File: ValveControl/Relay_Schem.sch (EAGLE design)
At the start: 69 parts, among them M1 IRLZ44, M2 IRLZ44, M3 IRLZ44, M4 IRLZ44, Q1 LINEAR_REGULATOR, Q2 LINEAR_REGULATOR, Q3 LINEAR_REGULATOR, Q4 LINEAR_REGULATOR, Q5 LINEAR_REGULATOR

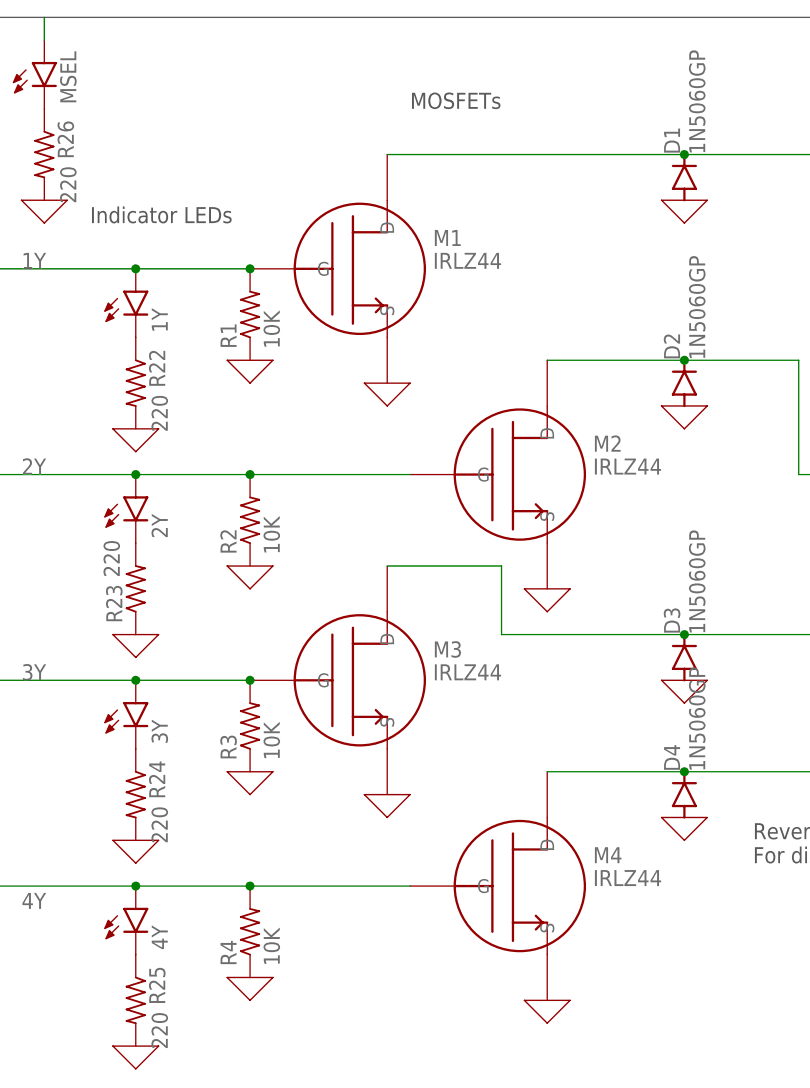
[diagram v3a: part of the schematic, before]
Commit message: Fix schematic errors, finish board layout
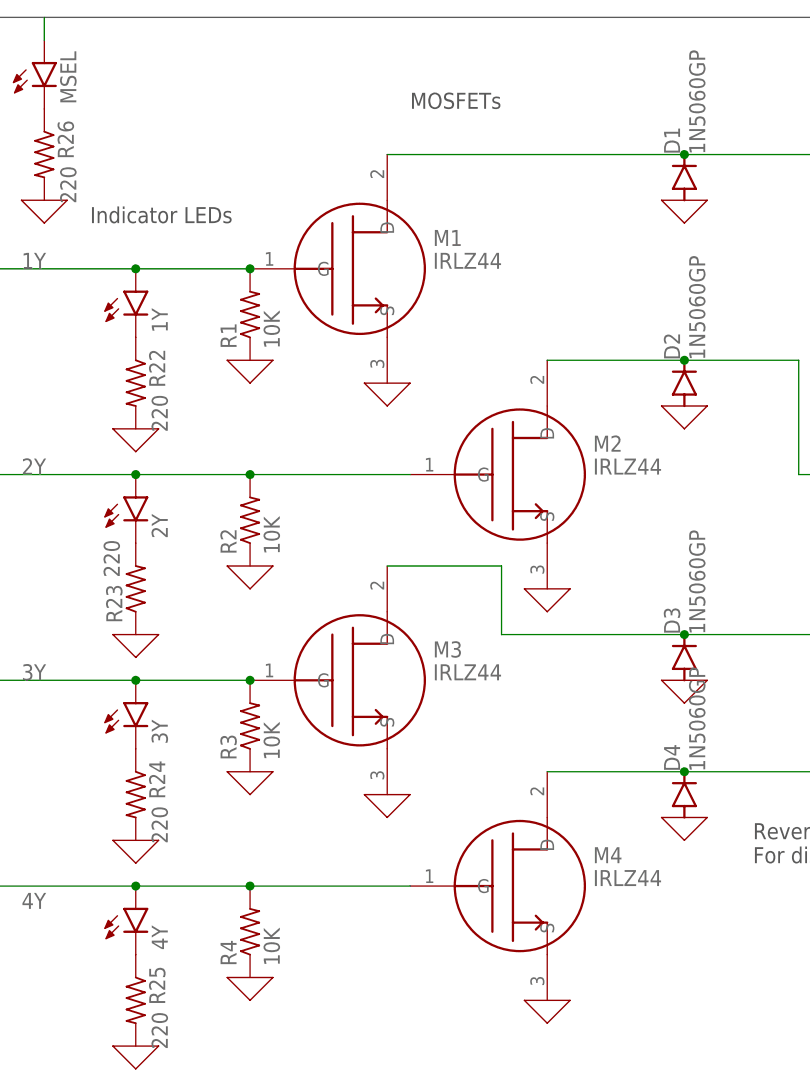
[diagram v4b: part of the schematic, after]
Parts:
- M1, M2, M3, M4: device ngspice-simulation:FET_N -> LPRD_RELAY:FET_N

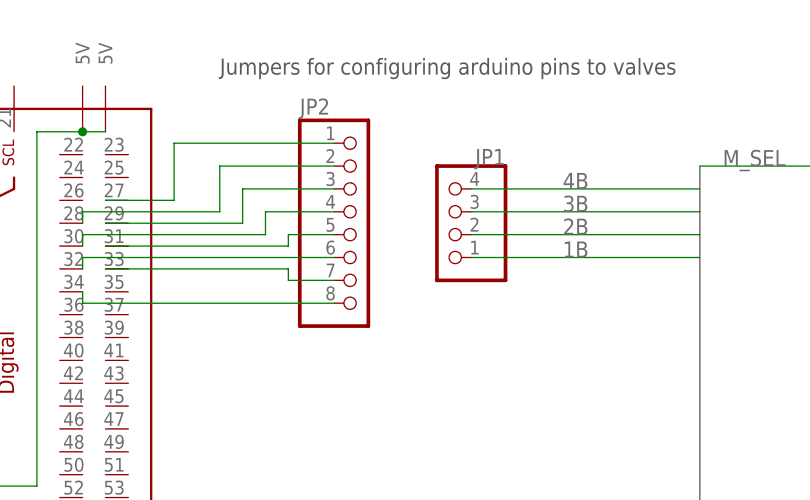
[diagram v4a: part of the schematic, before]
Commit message: Add pin numbers to valve pin selection jumper header
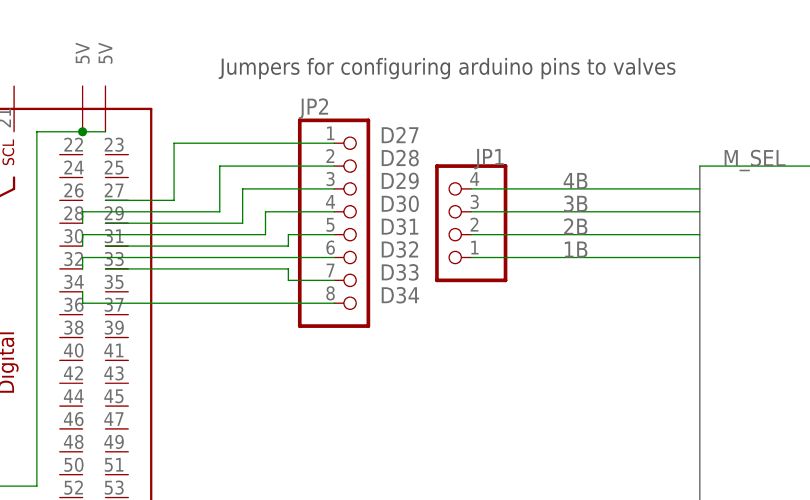
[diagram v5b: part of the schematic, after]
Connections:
- net N$25 renamed D27
- net N$26 renamed D28
- net N$27 renamed D29
- net N$28 renamed D30
- net N$29 renamed D31
- net N$30 renamed D32
- net N$31 renamed D33
- net N$32 renamed D34
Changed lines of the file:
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@@
 </segment>
 </net>
-<net name="N$25" class="0">
+<net name="D27" class="0">
 <segment>
 <pinref part="U$2" gate="G$1" pin="27"/>
@@
 <pinref part="JP2" gate="A" pin="1"/>
 <wire x1="48.26" y1="165.1" x2="66.04" y2="165.1" width="0.1524" layer="91"/>
+<label x="71.12" y="165.1" size="1.778" layer="95"/>
 </segment>
 </net>
-<net name="N$26" class="0">
+<net name="D28" class="0">
 <segment>
 <pinref part="U$2" gate="G$1" pin="28"/>
@@
 <pinref part="JP2" gate="A" pin="2"/>
 <wire x1="53.34" y1="162.56" x2="66.04" y2="162.56" width="0.1524" layer="91"/>
+<label x="71.12" y="162.56" size="1.778" layer="95"/>
 </segment>
 </net>
-<net name="N$27" class="0">
+<net name="D29" class="0">
 <segment>
 <pinref part="U$2" gate="G$1" pin="29"/>
@@
 <pinref part="JP2" gate="A" pin="3"/>
 <wire x1="55.88" y1="160.02" x2="66.04" y2="160.02" width="0.1524" layer="91"/>
+<label x="71.12" y="160.02" size="1.778" layer="95"/>
 </segment>
 </net>
-<net name="N$28" class="0">
+<net name="D30" class="0">
 <segment>
 <pinref part="U$2" gate="G$1" pin="30"/>
@@
 <pinref part="JP2" gate="A" pin="4"/>
 <wire x1="58.42" y1="157.48" x2="66.04" y2="157.48" width="0.1524" layer="91"/>
+<label x="71.12" y="157.48" size="1.778" layer="95"/>
 </segment>
 </net>
-<net name="N$29" class="0">
+<net name="D31" class="0">
 <segment>
 <pinref part="U$2" gate="G$1" pin="31"/>
@@
 <pinref part="JP2" gate="A" pin="5"/>
 <wire x1="60.96" y1="154.94" x2="66.04" y2="154.94" width="0.1524" layer="91"/>
+<label x="71.12" y="154.94" size="1.778" layer="95"/>
 </segment>
 </net>
-<net name="N$30" class="0">
+<net name="D32" class="0">
 <segment>
 <pinref part="U$2" gate="G$1" pin="32"/>
@@
 <wire x1="38.1" y1="151.13" x2="38.1" y2="152.4" width="0.1524" layer="91"/>
 <wire x1="38.1" y1="152.4" x2="66.04" y2="152.4" width="0.1524" layer="91"/>
+<label x="71.12" y="152.4" size="1.778" layer="95"/>
 </segment>
 </net>
-<net name="N$31" class="0">
+<net name="D33" class="0">
 <segment>
 <pinref part="U$2" gate="G$1" pin="33"/>
@@
 <pinref part="JP2" gate="A" pin="7"/>
 <wire x1="60.96" y1="149.86" x2="66.04" y2="149.86" width="0.1524" layer="91"/>
+<label x="71.12" y="149.86" size="1.778" layer="95"/>
 </segment>
 </net>
-<net name="N$32" class="0">
+<net name="D34" class="0">
 <segment>
 <pinref part="U$2" gate="G$1" pin="34"/>
@@
 <wire x1="38.1" y1="148.59" x2="38.1" y2="147.32" width="0.1524" layer="91"/>
 <wire x1="38.1" y1="147.32" x2="66.04" y2="147.32" width="0.1524" layer="91"/>
+<label x="71.12" y="147.32" size="1.778" layer="95"/>
 </segment>
 </net>

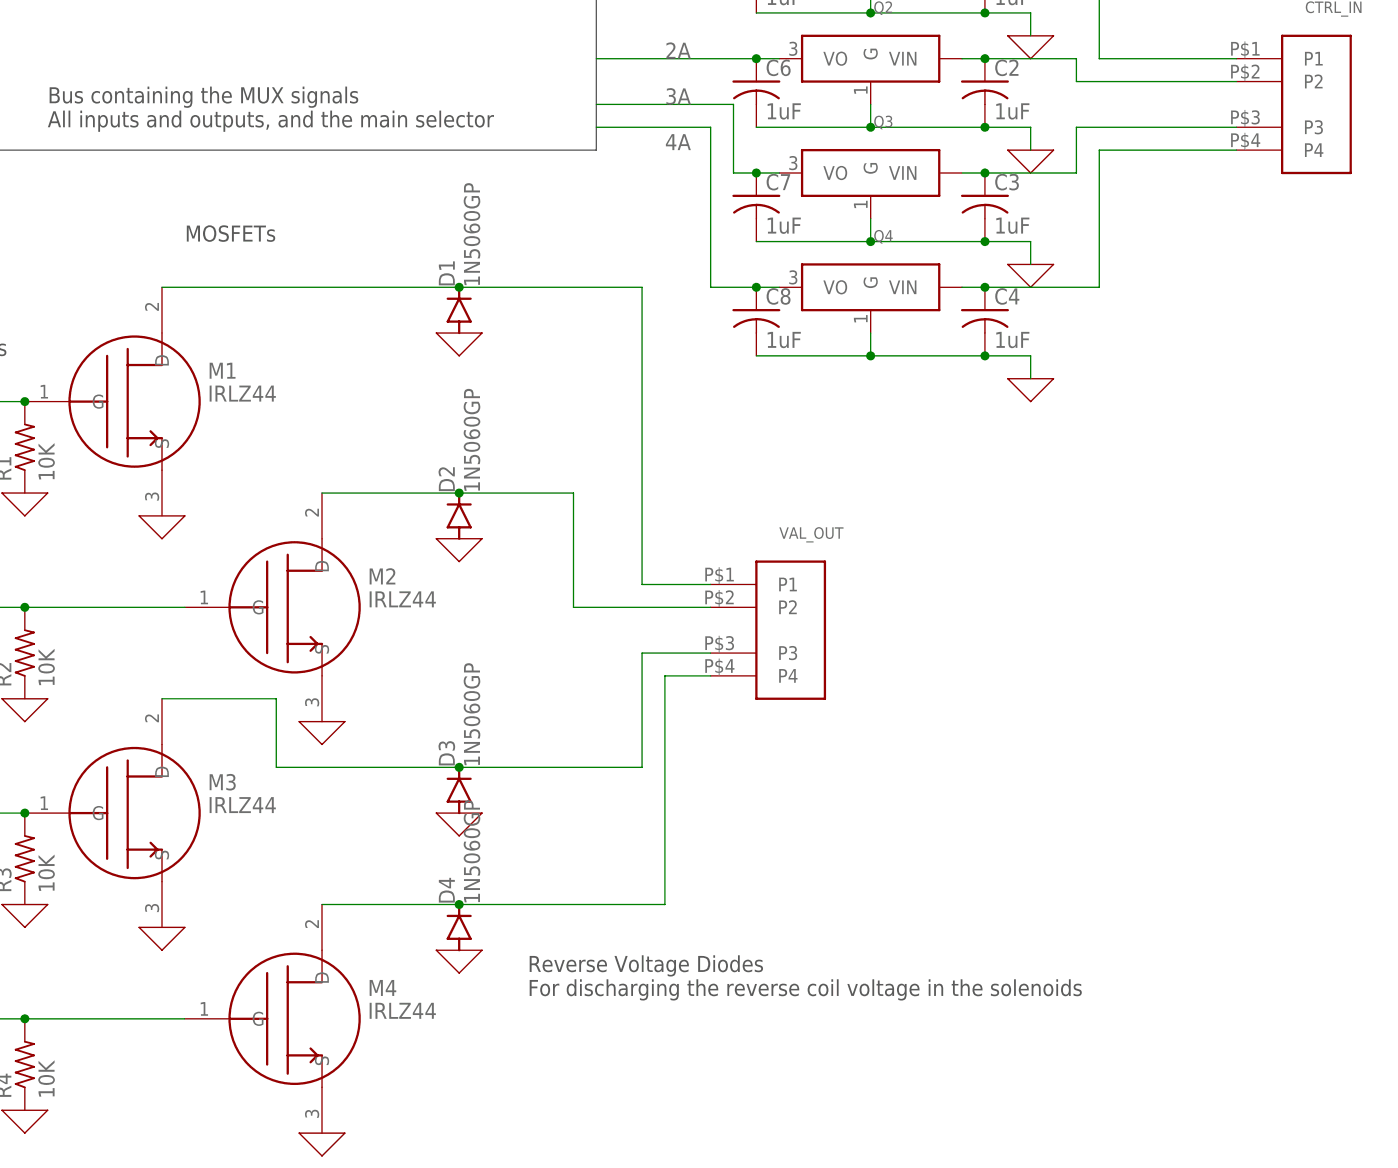
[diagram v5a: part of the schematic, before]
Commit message: Remove diodes, fix some slight layout issues
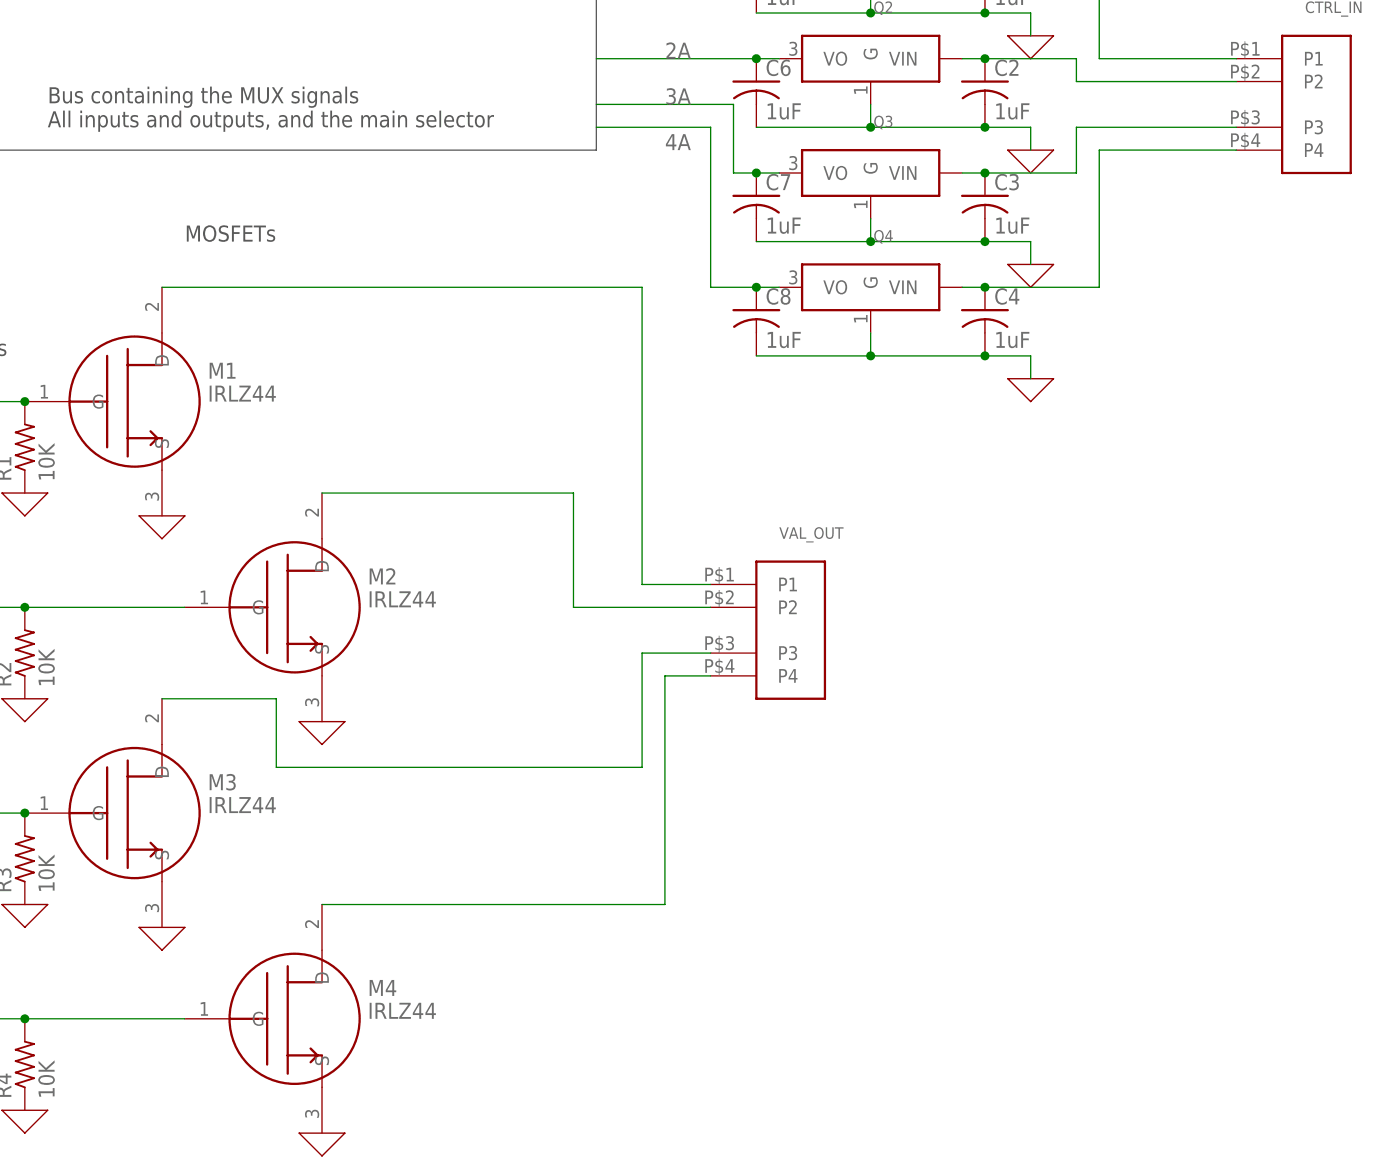
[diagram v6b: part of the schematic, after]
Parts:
- removed D1, D2, D3, D4: 1N5060GP, diode:1N5060GP
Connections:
- net 0: no longer D1.A, D2.A, D3.A, D4.A
- net N$3: no longer D1.C
- net N$5: no longer D2.C
- net N$8: no longer D3.C
- net N$9: no longer D4.C
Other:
- note removed: "Reverse Voltage Diodes For discharging the reverse coil voltage in the solenoids"
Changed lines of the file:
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@@
 <part name="R24" library="rcl" library_urn="urn:adsk.eagle:library:334" deviceset="R-US_" device="0204/7" package3d_urn="urn:adsk.eagle:package:23498/2" value="220"/>
 <part name="R25" library="rcl" library_urn="urn:adsk.eagle:library:334" deviceset="R-US_" device="0204/7" package3d_urn="urn:adsk.eagle:package:23498/2" value="220"/>
-<part name="D1" library="diode" library_urn="urn:adsk.eagle:library:210" deviceset="1N5060GP" device="" package3d_urn="urn:adsk.eagle:package:43369/2"/>
-<part name="D2" library="diode" library_urn="urn:adsk.eagle:library:210" deviceset="1N5060GP" device="" package3d_urn="urn:adsk.eagle:package:43369/2"/>
-<part name="D3" library="diode" library_urn="urn:adsk.eagle:library:210" deviceset="1N5060GP" device="" package3d_urn="urn:adsk.eagle:package:43369/2"/>
-<part name="D4" library="diode" library_urn="urn:adsk.eagle:library:210" deviceset="1N5060GP" device="" package3d_urn="urn:adsk.eagle:package:43369/2"/>
-<part name="X_15" library="ngspice-simulation" library_urn="urn:adsk.eagle:library:527439" deviceset="GND" device=""/>
 <part name="MSEL" library="led" library_urn="urn:adsk.eagle:library:259" deviceset="LED" device="3MM" package3d_urn="urn:adsk.eagle:package:15797/1"/>
 <part name="R26" library="rcl" library_urn="urn:adsk.eagle:library:334" deviceset="R-US_" device="0204/7" package3d_urn="urn:adsk.eagle:package:23498/2" value="220"/>
@@
 <part name="X_25" library="ngspice-simulation" library_urn="urn:adsk.eagle:library:527439" deviceset="GND" device=""/>
 <part name="X_26" library="ngspice-simulation" library_urn="urn:adsk.eagle:library:527439" deviceset="GND" device=""/>
-<part name="X_27" library="ngspice-simulation" library_urn="urn:adsk.eagle:library:527439" deviceset="GND" device=""/>
-<part name="X_28" library="ngspice-simulation" library_urn="urn:adsk.eagle:library:527439" deviceset="GND" device=""/>
-<part name="X_29" library="ngspice-simulation" library_urn="urn:adsk.eagle:library:527439" deviceset="GND" device=""/>
 <part name="JP1" library="pinhead" library_urn="urn:adsk.eagle:library:325" deviceset="PINHD-1X4" device="" package3d_urn="urn:adsk.eagle:package:22407/2"/>
 <part name="JP2" library="pinhead" library_urn="urn:adsk.eagle:library:325" deviceset="PINHD-1X8" device="" package3d_urn="urn:adsk.eagle:package:22409/2"/>
@@
 <sheet>
 <plain>
-<text x="99.06" y="-7.62" size="1.778" layer="97">Reverse Voltage Diodes
-For discharging the reverse coil voltage in the solenoids</text>
 <text x="60.96" y="76.2" size="1.778" layer="97">MOSFETs</text>
 <text x="-106.68" y="71.12" size="1.778" layer="97">Indicator LEDs</text>
@@
 <attribute name="VALUE" x="32.258" y="-24.13" size="1.778" layer="96" rot="R270"/>
 </instance>
-<instance part="D1" gate="1" x="91.44" y="68.58" smashed="yes" rot="R90">
-<attribute name="NAME" x="90.9574" y="71.12" size="1.778" layer="95" rot="R90"/>
-<attribute name="VALUE" x="93.7514" y="71.12" size="1.778" layer="96" rot="R90"/>
-</instance>
-<instance part="D2" gate="1" x="91.44" y="45.72" smashed="yes" rot="R90">
-<attribute name="NAME" x="90.9574" y="48.26" size="1.778" layer="95" rot="R90"/>
-<attribute name="VALUE" x="93.7514" y="48.26" size="1.778" layer="96" rot="R90"/>
-</instance>
-<instance part="D3" gate="1" x="91.44" y="15.24" smashed="yes" rot="R90">
-<attribute name="NAME" x="90.9574" y="17.78" size="1.778" layer="95" rot="R90"/>
-<attribute name="VALUE" x="93.7514" y="17.78" size="1.778" layer="96" rot="R90"/>
-</instance>
-<instance part="D4" gate="1" x="91.44" y="0" smashed="yes" rot="R90">
-<attribute name="NAME" x="90.9574" y="2.54" size="1.778" layer="95" rot="R90"/>
-<attribute name="VALUE" x="93.7514" y="2.54" size="1.778" layer="96" rot="R90"/>
-</instance>
-<instance part="X_15" gate="G$1" x="91.44" y="-2.54" smashed="yes"/>
 <instance part="MSEL" gate="G$1" x="20.32" y="81.28" smashed="yes">
 <attribute name="NAME" x="23.876" y="76.708" size="1.778" layer="95" rot="R90"/>
@@
 <instance part="X_25" gate="G$1" x="58.42" y="0" smashed="yes"/>
 <instance part="X_26" gate="G$1" x="76.2" y="-22.86" smashed="yes"/>
-<instance part="X_27" gate="G$1" x="91.44" y="66.04" smashed="yes"/>
-<instance part="X_28" gate="G$1" x="91.44" y="12.7" smashed="yes"/>
-<instance part="X_29" gate="G$1" x="91.44" y="43.18" smashed="yes"/>
 <instance part="JP1" gate="A" x="78.74" y="157.48" smashed="yes" rot="R180">
 <attribute name="NAME" x="85.09" y="164.465" size="1.778" layer="95" rot="R180"/>
@@
 </segment>
 <segment>
-<pinref part="D4" gate="1" pin="A"/>
-<pinref part="X_15" gate="G$1" pin="0"/>
-</segment>
-<segment>
-<pinref part="X_27" gate="G$1" pin="0"/>
-<pinref part="D1" gate="1" pin="A"/>
-</segment>
-<segment>
-<pinref part="X_28" gate="G$1" pin="0"/>
-<pinref part="D3" gate="1" pin="A"/>
-</segment>
-<segment>
-<pinref part="X_29" gate="G$1" pin="0"/>
-<pinref part="D2" gate="1" pin="A"/>
-</segment>
-<segment>
 <pinref part="R22" gate="G$1" pin="2"/>
 <pinref part="X_19" gate="G$1" pin="0"/>
@@
 <wire x1="111.76" y1="17.78" x2="111.76" y2="30.48" width="0.1524" layer="91"/>
 <wire x1="111.76" y1="30.48" x2="119.38" y2="30.48" width="0.1524" layer="91"/>
-<pinref part="D3" gate="1" pin="C"/>
-<wire x1="91.44" y1="17.78" x2="111.76" y2="17.78" width="0.1524" layer="91"/>
 <pinref part="VAL_OUT" gate="G$1" pin="P3"/>
 <wire x1="58.42" y1="25.4" x2="71.12" y2="25.4" width="0.1524" layer="91"/>
 <wire x1="71.12" y1="25.4" x2="71.12" y2="17.78" width="0.1524" layer="91"/>
-<wire x1="71.12" y1="17.78" x2="91.44" y2="17.78" width="0.1524" layer="91"/>
-<junction x="91.44" y="17.78"/>
+<wire x1="71.12" y1="17.78" x2="111.76" y2="17.78" width="0.1524" layer="91"/>
 <pinref part="M3" gate="G$1" pin="D"/>
 </segment>
@@
 <wire x1="114.3" y1="2.54" x2="114.3" y2="27.94" width="0.1524" layer="91"/>
 <wire x1="114.3" y1="27.94" x2="119.38" y2="27.94" width="0.1524" layer="91"/>
-<wire x1="76.2" y1="2.54" x2="91.44" y2="2.54" width="0.1524" layer="91"/>
-<pinref part="D4" gate="1" pin="C"/>
-<wire x1="91.44" y1="2.54" x2="114.3" y2="2.54" width="0.1524" layer="91"/>
-<junction x="91.44" y="2.54"/>
+<wire x1="76.2" y1="2.54" x2="114.3" y2="2.54" width="0.1524" layer="91"/>
 <pinref part="VAL_OUT" gate="G$1" pin="P4"/>
 <pinref part="M4" gate="G$1" pin="D"/>
@@
 <wire x1="111.76" y1="71.12" x2="111.76" y2="38.1" width="0.1524" layer="91"/>
 <wire x1="111.76" y1="38.1" x2="119.38" y2="38.1" width="0.1524" layer="91"/>
-<wire x1="111.76" y1="71.12" x2="91.44" y2="71.12" width="0.1524" layer="91"/>
-<pinref part="D1" gate="1" pin="C"/>
-<wire x1="91.44" y1="71.12" x2="58.42" y2="71.12" width="0.1524" layer="91"/>
-<junction x="91.44" y="71.12"/>
+<wire x1="111.76" y1="71.12" x2="58.42" y2="71.12" width="0.1524" layer="91"/>
 <pinref part="VAL_OUT" gate="G$1" pin="P1"/>
 <pinref part="M1" gate="G$1" pin="D"/>
@@
 <net name="N$5" class="0">
 <segment>
-<pinref part="D2" gate="1" pin="C"/>
-<wire x1="76.2" y1="48.26" x2="91.44" y2="48.26" width="0.1524" layer="91"/>
-<wire x1="91.44" y1="48.26" x2="104.14" y2="48.26" width="0.1524" layer="91"/>
-<junction x="91.44" y="48.26"/>
+<wire x1="76.2" y1="48.26" x2="104.14" y2="48.26" width="0.1524" layer="91"/>
 <pinref part="VAL_OUT" gate="G$1" pin="P2"/>
 <wire x1="104.14" y1="48.26" x2="104.14" y2="35.56" width="0.1524" layer="91"/>
